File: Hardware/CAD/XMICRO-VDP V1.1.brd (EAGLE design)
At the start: 203.2 x 101.6 mm, 87 parts, among them J1 PJRAN1XU04AUX, J2 MINI-DIN4, J4 PINHD-2X6, J5 PINHD-1X8, Q1 VN2106, Q2 VN2106, U1 74574, U10 7414, U11 7404, U12 74244, U13 7432, U14 74574, U15 74244, U16 74245, U17 V9958, U18 CXA2075, U2 AS6C4008, U3 74574, U4 74574, U5 7404, U6 7410, U7 74138, U8 74373, U9 7474, Y1 5MHz, Y2 21.47727MHz

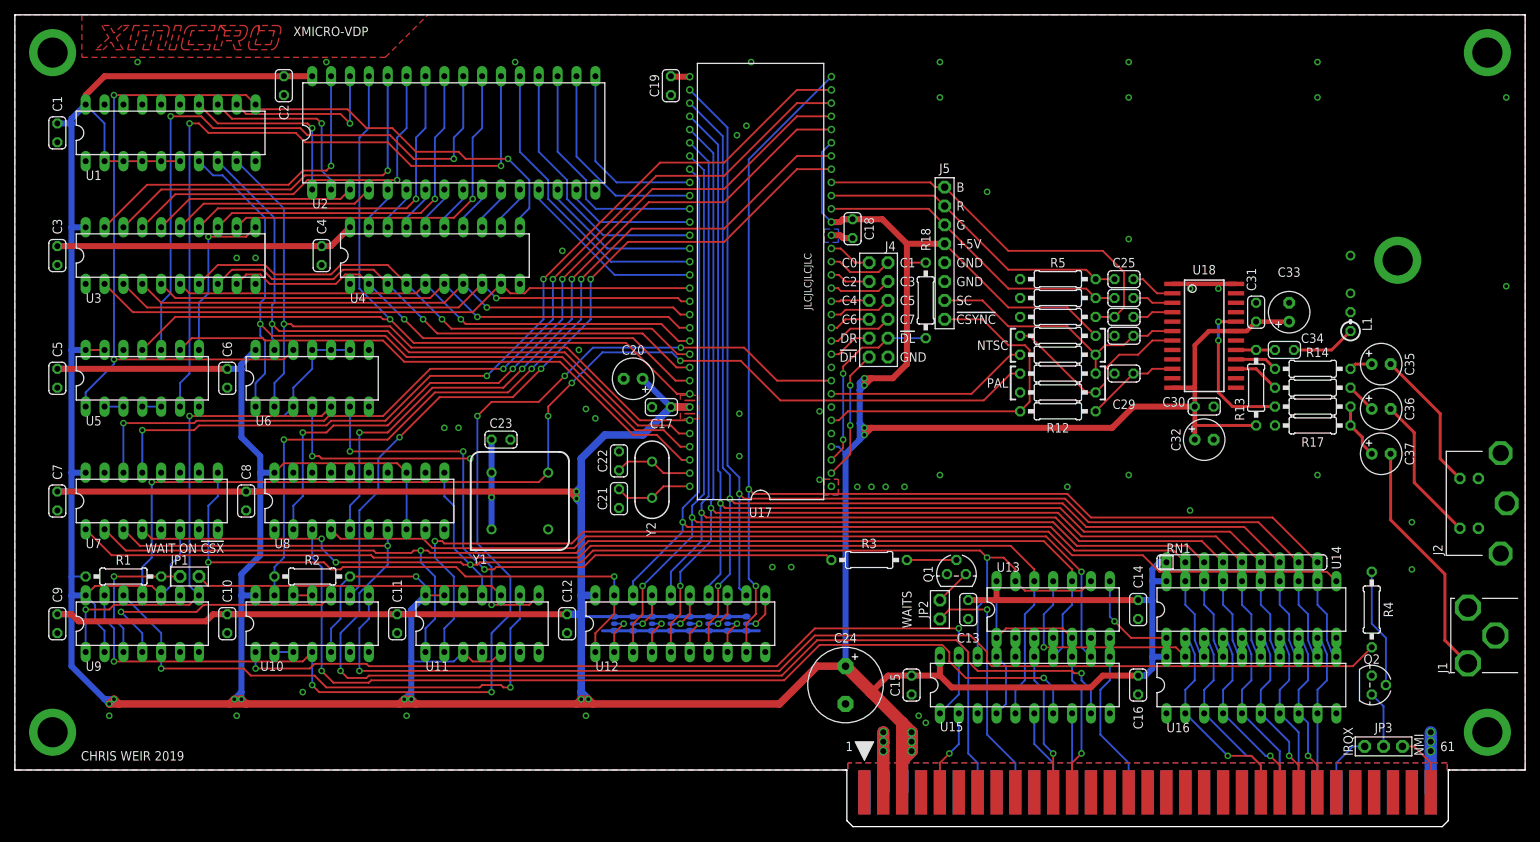
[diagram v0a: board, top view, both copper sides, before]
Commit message: Updated to XMICRO-VDP V1.1. Replaced VRAM with dynamic RAM, various other minor tweaks.
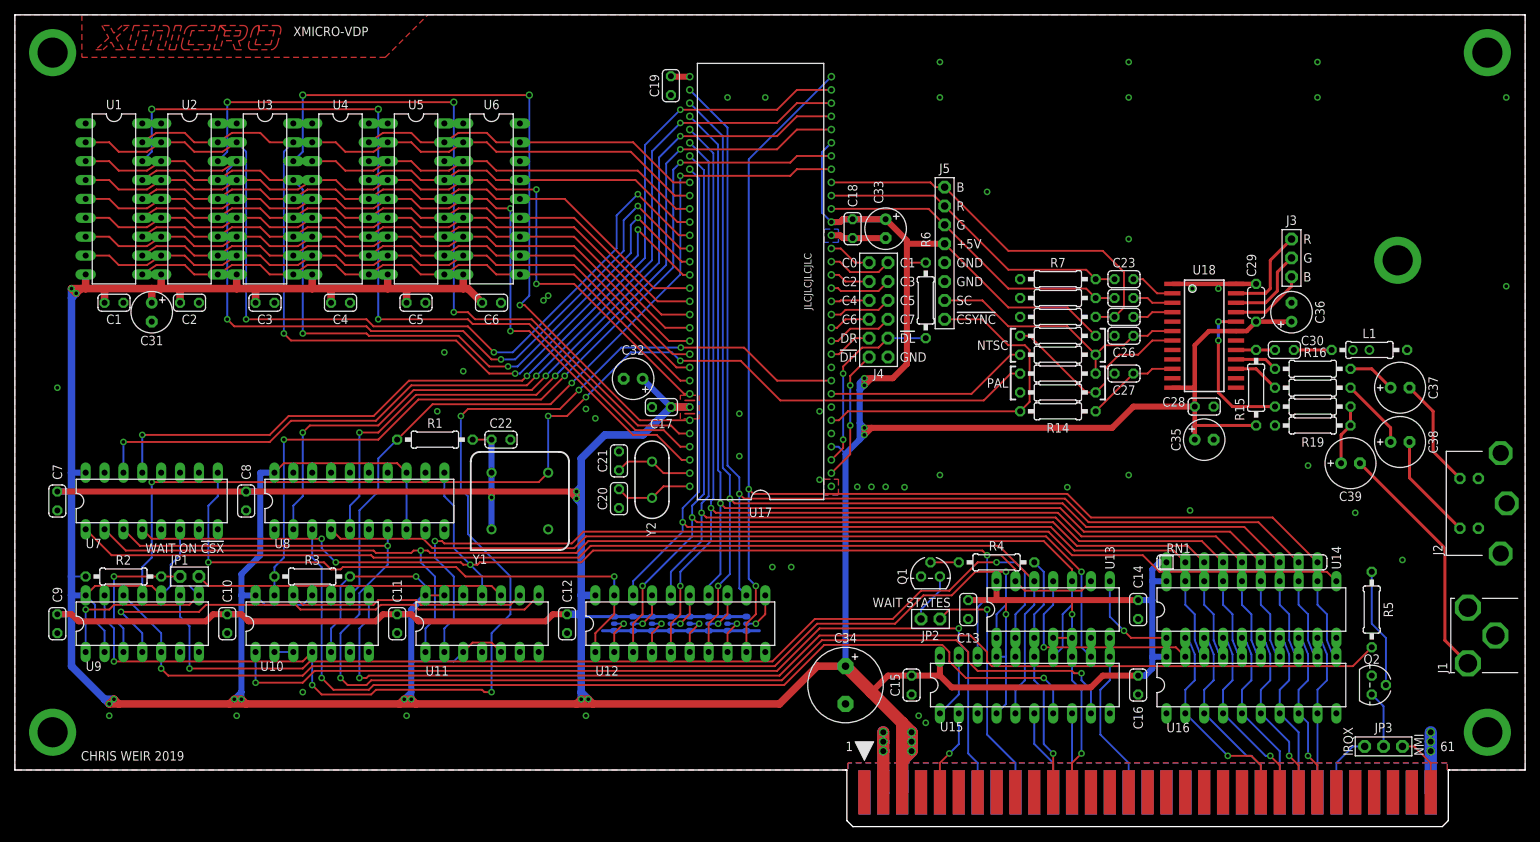
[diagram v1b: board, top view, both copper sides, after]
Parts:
- added C38, C39: 220uF, rcl:E2,5-7
- added J3: PINHD1X3, Custom:1X03
- added R19: 240, rcl:0207/10
- C20: value 47uF -> 22pF; device rcl:E2,5-6 -> Custom:C100
- C22: value 22pF -> 0.1uF
- C24: value 220uF -> 0.1uF; device Custom:C-10-5 -> Custom:C100
- C26: value 0.1uF -> 5pF
- C27: value 0.1uF -> 47pF
- C28: value 5pF -> 10nF
- C29: value 47pF -> 10nF; device Custom:C100 -> rcl:C050-024X044
- C30: value 10nF -> 28pF
- C31: value 10nF -> 47uF; device Custom:C100 -> rcl:E2,5-6
- C34: value 28pF -> 470uF; device Custom:C100 -> Custom:C-10-5
- C35, C36: value 220uF -> 47uF
- C37: device rcl:E2,5-6 -> rcl:E2,5-7
- L1: device rcl:0204V -> rcl:0207/10
- R1, RN1: value 10k -> 3.3k
- R10: value 2.2k -> 0
- R11: value 0 -> 2.2k
- R13: value 3.32k/1% -> 0
- R14: value 75 -> 2.2k
- R15: value 75 -> 3.32k/1%
- R16: value 43 -> 75
- R17: value 240 -> 75
- R18: value 3.3k -> 43
- R2: value 3.3k -> 10k
- R3: value 0 -> 3.3k
- R5: value 470 -> 0
- R6: value 470 -> 3.3k
- R8: value 0 -> 470
- R9: value 2.2k -> 470
- U1, U3, U4: value 74574 -> 41464; device 74xx-us:DIL20 -> Custom:DIL18
- U2: value AS6C4008 -> 41464; device Custom:DIL32-6 -> Custom:DIL18
- U5: value 7404 -> 41464; device 74xx-us:DIL14 -> Custom:DIL18
- U6: value 7410 -> 41464; device 74xx-us:DIL14 -> Custom:DIL18
- moved C31 148.6 mm to (18.4, 61.6), turned to 270 degrees
- moved C23 86.6 mm to (149.2, 66.0)
- moved C32 77.3 mm to (83.2, 52.6), turned to 180 degrees
- moved R3 75.0 mm to (40.0, 26.0)
- moved C34 74.3 mm to (111.8, 11.4), turned to 270 degrees
- moved C24 64.1 mm to (149.2, 63.5), turned to 0 degrees
- moved R5 61.3 mm to (182.6, 21.6), turned to 90 degrees
- moved C33 55.4 mm to (117.2, 72.8), turned to 270 degrees
- moved R18 54.0 mm to (174.6, 48.9), turned to 0 degrees
- moved R4 50.9 mm to (132.1, 27.9), turned to 180 degrees
- moved C5 49.3 mm to (54.0, 62.9), turned to 0 degrees
- moved R1 45.8 mm to (56.5, 44.5), turned to 0 degrees
- moved U5 44.0 mm to (54.0, 76.8), turned to 270 degrees
- moved C6 37.0 mm to (64.1, 62.9), turned to 0 degrees
- moved U2 36.7 mm to (23.5, 76.8), turned to 270 degrees
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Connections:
- removed net N$31: U3.11, U5.8
- removed net N$32: U2.12, U4.12
- removed net N$41: U2.11, U4.13
- removed net N$42: U2.10, U4.14
- removed net N$43: U2.9, U4.15
- removed net N$44: U2.8, U4.16
- removed net N$45: U2.7, U4.17
- removed net N$46: U2.6, U4.18
- removed net N$47: U2.5, U4.19
- removed net N$48: U1.11, U4.11, U5.1, U6.12
- removed net N$49: U2.24, U5.10
- removed net N$50: U2.22, U5.6
- removed net N$57: U2.23, U3.12
- removed net N$58: U2.25, U3.13
- removed net N$59: U2.26, U3.14
- removed net N$60: U2.4, U3.15
- removed net N$61: U2.3, U3.16
- removed net N$62: U2.27, U3.17
- removed net N$63: U2.28, U3.18
- removed net N$64: U2.31, U3.19
- removed net N$65: U1.13, U2.2
- removed net N$66: U1.12, U2.30
- removed net N$67: U1.14, U2.1
- removed net N$76: U5.2, U5.3
- removed net N$78: U11.8, U6.4
- removed net N$80: U5.4, U5.5
- new net N$1: U13.2, U9.9
- new net N$2: J3.3, U18.21
- new net N$6: J3.2, U18.22
- new net N$7: J3.1, U18.23
- net !CSYNC: now also R14.1; no longer R12.1
- net !DLCLK: now also R6.1; no longer R18.1
- net !VCAS0: now also U1.16, U4.16; no longer U1.7, U6.1
- net !VCAS1: now also U2.16, U5.16; no longer U1.8, U6.13
- net !VCAS2: now also U3.16, U6.16; no longer U1.9, U6.2
- net !VINT: now also R1.1
- net !VRAS: now also U1.5, U2.5, U3.5, U4.5, U5.5, U6.5; no longer U5.9
- net !VWAIT: now also R3.1; no longer R2.1
- net B: now also C25.P$1, R9.2; no longer C27.P$1, R7.2
- net G: now also C24.P$1, R8.2; no longer C26.P$1, R6.2
- net GND: now also C20.P$2, C26.P$2, C27.P$2, C29.2, C31.-, C34.-, C35.-, C36.-, R13.2, R19.1, R8.1, R9.1, U1.18, U2.1, U2.18, U3.18, U4.18, U5.1, U5.18, U6.1, U6.18; no longer C20.-, C23.P$2, C24.-, C29.P$2, C30.P$2, C31.P$2, R11.2, R17.1, R5.1, R6.1, U1.10, U2.16, U3.10, U4.10, U5.7, U6.7
- net N$11: now also R5.1; no longer R4.1
- net N$12: now also R17.1; no longer R15.1
- net N$13: now also R16.1; no longer R14.1
- net N$14: now also R18.1; no longer R16.1
- net N$15: now also C39.+, R18.2, R19.2; no longer C37.+, R16.2, R17.2
- net N$16: now also C37.+, R16.2; no longer C35.+, R14.2
- net N$17: now also C38.+, R17.2; no longer C36.+, R15.2
- net N$19: now also U11.8; no longer U10.10
- net N$20: now also U11.9; no longer U10.11
- net N$21: now also C30.P$2; no longer C34.P$2
- net N$22: now also C27.P$1, R14.2; no longer C29.P$1, R12.2
- net N$26: now also R10.1, R13.1; no longer R11.1, R8.1
- net N$28: now also C21.P$1; no longer C22.P$1
- net N$29: now also C38.-; no longer C36.-
- net N$3: now also C23.P$2; no longer C25.P$2
- net N$30: now also C20.P$1; no longer C21.P$1
- net N$4: now also C24.P$2; no longer C26.P$2
- net N$5: now also C25.P$2; no longer C27.P$2
- net N$51: now also R4.2; no longer R3.2
- net N$53: now also C39.-; no longer C37.-
- net N$71: now also C30.P$1, R15.2; no longer C34.P$1, R13.2
- net N$73: now also R4.1, U13.3; no longer R3.1, U6.6
- net N$77: now also U13.1; no longer U11.9
- net N$79: no longer U6.5
- net N$81: now also C37.-; no longer C35.-
- net N$83: now also R2.1; no longer R1.1
- net N$9: now also R5.2; no longer R4.2
- net NTSC_SC: now also R11.1; no longer R9.1
- net PAL_SC: now also R12.1; no longer R10.1
- net R: now also C23.P$1, R7.2; no longer C25.P$1, R5.2
- net SC: now also C26.P$1, R11.2, R12.2; no longer C28.P$1, R10.2, R9.2
- net VA0: now also U1.14, U2.14, U3.14, U4.14, U5.14, U6.14; no longer U3.2, U4.9
- net VA1: now also U1.13, U2.13, U3.13, U4.13, U5.13, U6.13; no longer U3.3, U4.8
- net VA2: now also U1.6, U2.6, U3.6, U4.6, U5.6, U6.6; no longer U3.4, U4.7
- net VA3: now also U1.12, U2.12, U3.12, U4.12, U5.12, U6.12; no longer U3.5, U4.6
- net VA4: now also U1.7, U2.7, U3.7, U4.7, U5.7, U6.7; no longer U3.6, U4.5
- net VA5: now also U1.11, U2.11, U3.11, U4.11, U5.11, U6.11; no longer U3.7, U4.4
- net VA6: now also U1.8, U2.8, U4.8, U5.8, U6.8; no longer U4.3
- net VA7: now also U1.10, U2.10, U3.10, U4.10, U5.10, U6.10; no longer U3.9, U4.2
- net VCC: now also C22.P$1, C28.P$1, C29.1, C31.+, C34.+, C35.+, C36.+, R10.2, R15.1, R3.2, R6.2, U1.9, U10.11, U2.9, U3.9, U4.9, U5.9; no longer C20.+, C23.P$1, C24.+, C30.P$1, C31.P$1, R13.1, R18.2, R8.2, U1.2, U1.20, U1.3, U1.4, U1.5, U1.6, U13.1, U13.2, U2.32, U3.20, U4.20, U5.13, U5.14, U6.10, U6.11, U6.14, U6.3
- net VD0: now also U4.17, U5.17, U6.17; no longer U2.17
- net VD1: now also U4.2, U5.2, U6.2; no longer U2.18
- net VD2: now also U4.3, U5.3, U6.3; no longer U2.19
- net VD3: now also U4.15, U5.15, U6.15; no longer U2.15
- net VD4: now also U1.2, U2.2, U3.2; no longer U2.20
- net VD5: now also U1.3, U2.3, U3.3; no longer U2.14
- net VD6: now also U1.15, U2.15, U3.15; no longer U2.21
- net VD7: now also U1.17, U2.17, U3.17; no longer U2.13
- net VR/!W: now also U1.4, U2.4, U3.4, U4.4, U5.4, U6.4; no longer U2.29, U5.11
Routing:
- net N$1: track 0.00 -> 138.6 mm, vias 0 -> 2
- net N$48: track 135.6 -> 0.00 mm, vias 3 -> 0
- net VCC: track 1157.5 -> 1055.8 mm, vias 19 -> 23
- net VD5: track 21.8 -> 121.7 mm, vias 0 -> 3
- net N$50: track 95.0 -> 0.00 mm, vias 2 -> 0
- net VD7: track 25.8 -> 117.8 mm, vias 0 -> 3
- net VD4: track 36.6 -> 121.7 mm, vias 0 -> 3
- net N$49: track 84.1 -> 0.00 mm, vias 2 -> 0
- net N$73: track 86.1 -> 11.2 mm, vias 3 -> 0
- net VD6: track 40.6 -> 110.2 mm, vias 0 -> 3
- net N$77: track 73.2 -> 141.2 mm
- net N$78: track 55.8 -> 0.00 mm, vias 3 -> 0
- net N$62: track 51.4 -> 0.00 mm, vias 1 -> 0
- net N$63: track 51.4 -> 0.00 mm, vias 1 -> 0
- net N$57: track 50.4 -> 0.00 mm, vias 1 -> 0
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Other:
- board text added: "V1.1 1949"
- board text added: "WAIT STATES"
- board text removed: "V1 1946"
- board text removed: "WAITS"
